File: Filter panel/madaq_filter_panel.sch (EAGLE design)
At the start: 34 parts

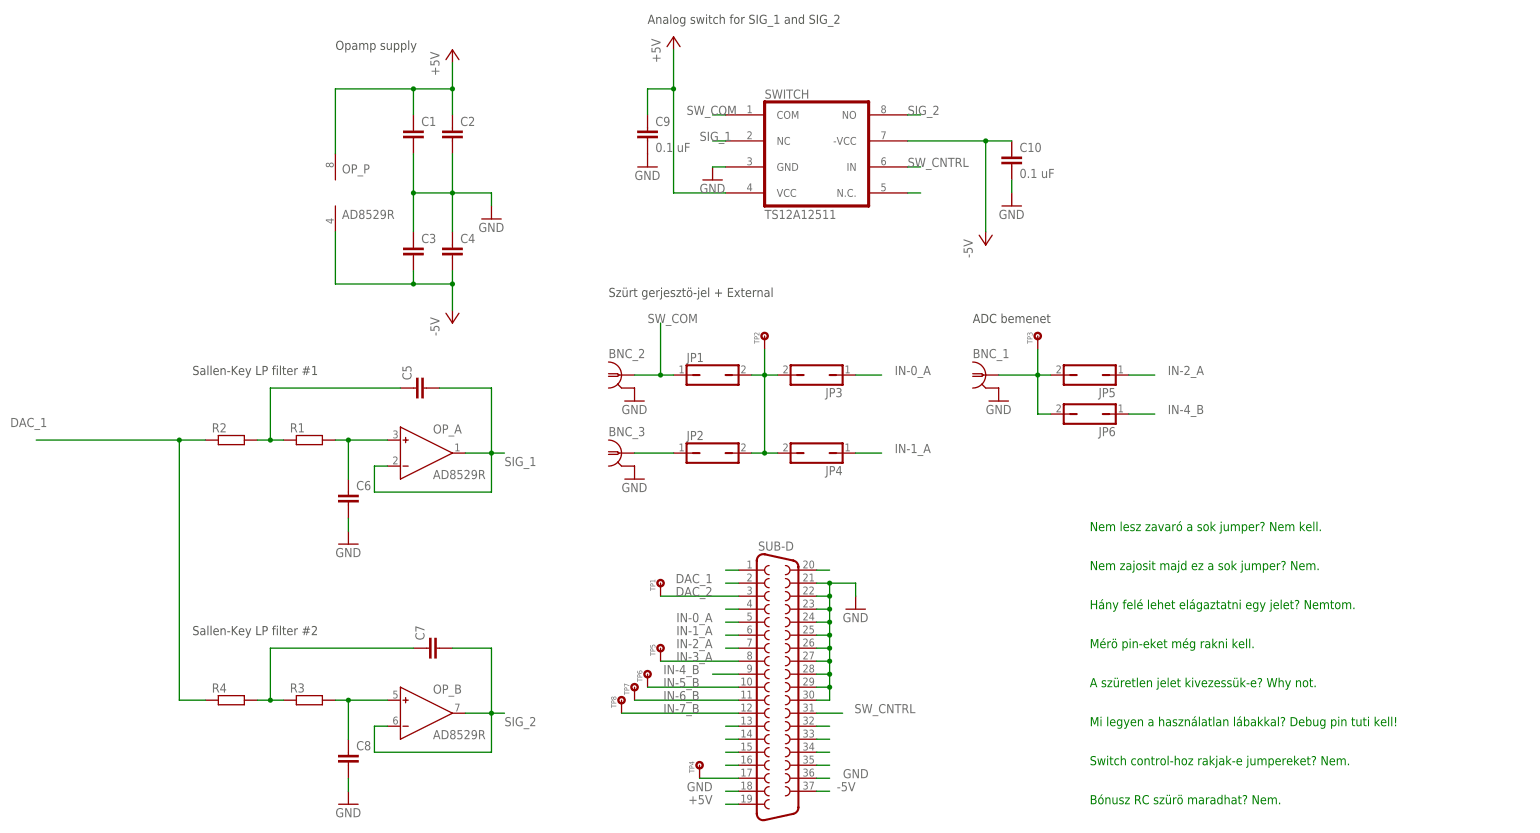
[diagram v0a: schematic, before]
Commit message: Filter panel - V4 sch + brd, Robi és János átnézte - ez nem a megrendelt verzió (János még babrált a board-on)
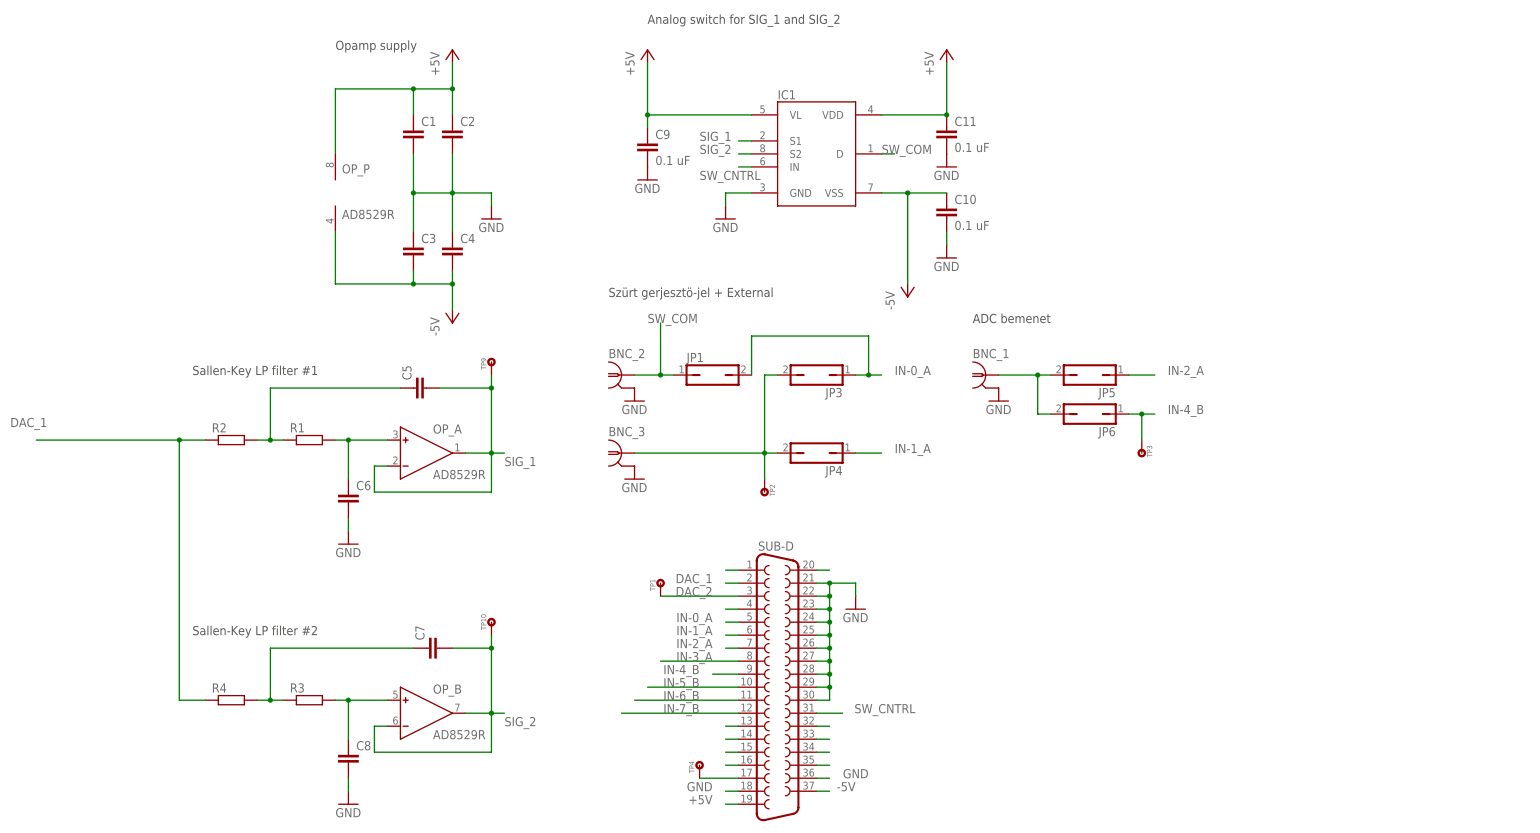
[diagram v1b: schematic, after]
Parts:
- removed JP2: (no value), jumper:JP1Q
- removed SWITCH: TS12A12511, Zoli2_2015-02-22:TS12A12511
- removed TP5, TP6, TP7, TP8: TP, MRobi:TP
- added C11: 0.1 uF, Zoli2_2015-01-28:C1206
- added IC1: (no value), MRobi:ADG419BR
- added TP10, TP9: TP, MRobi:TP
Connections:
- removed net N$2: SWITCH.N.C.
- removed net N$7: JP1.2, JP2.2, JP3.2, JP4.2, TP2.1
- net +5V: now also C11.2, IC1.VDD, IC1.VL; no longer SWITCH.VCC
- net -5V: now also IC1.VSS; no longer SWITCH.-VCC
- net GND: now also C11.1, IC1.GND; no longer SWITCH.GND
- net IN-0_A: now also JP1.2
- net IN-3_A: no longer TP5.1
- net IN-4_B: now also TP3.1
- net IN-5_B: no longer TP6.1
- net IN-6_B: no longer TP7.1
- net IN-7_B: no longer TP8.1
- net N$8: no longer TP3.1
- net N$9: now also JP3.2, JP4.2, TP2.1; no longer JP2.1
- net SIG_1: now also IC1.S1, TP9.1; no longer SWITCH.NC
- net SIG_2: now also IC1.S2, TP10.1; no longer SWITCH.NO
- net SW_CNTRL: now also IC1.IN; no longer SWITCH.IN
- net SW_COM: now also IC1.D; no longer SWITCH.COM
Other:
- note removed: "A szüretlen jelet kivezessük-e? Why not."
- note removed: "Bónusz RC szürö maradhat? Nem."
- note removed: "Hány felé lehet elágaztatni egy jelet? Nemtom."
- note removed: "Mi legyen a használatlan lábakkal? Debug pin tuti kell!"
- note removed: "Mérö pin-eket még rakni kell."
- note removed: "Nem lesz zavaró a sok jumper? Nem kell."
- note removed: "Nem zajosit majd ez a sok jumper? Nem."
- note removed: "Switch control-hoz rakjak-e jumpereket? Nem."
- moved on the sheet: C10, C9, TP2, TP3

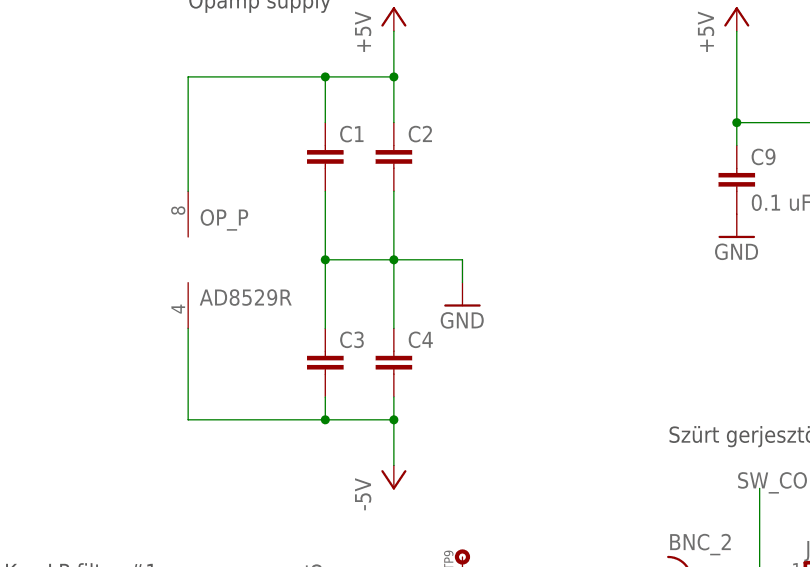
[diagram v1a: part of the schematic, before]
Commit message: Filter panel - János upgraded version, R C értékek még kellenek
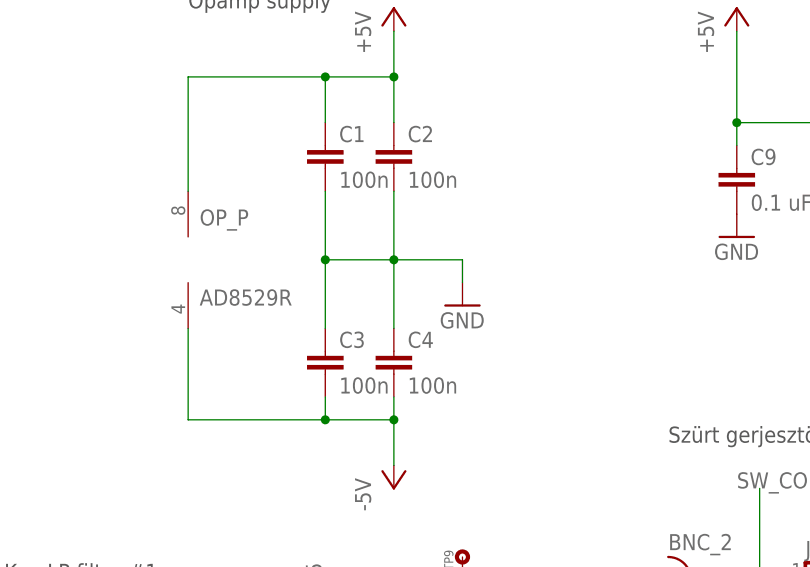
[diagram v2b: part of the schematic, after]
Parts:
- C1, C2, C3, C4: value (none) -> 100n
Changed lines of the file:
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@@
 </classes>
 <parts>
-<part name="C1" library="Zoli2_2015-01-28" deviceset="C" device="1206"/>
-<part name="C2" library="Zoli2_2015-01-28" deviceset="C" device="1206"/>
-<part name="C3" library="Zoli2_2015-01-28" deviceset="C" device="1206"/>
-<part name="C4" library="Zoli2_2015-01-28" deviceset="C" device="1206"/>
+<part name="C1" library="Zoli2_2015-01-28" deviceset="C" device="1206" value="100n"/>
+<part name="C2" library="Zoli2_2015-01-28" deviceset="C" device="1206" value="100n"/>
+<part name="C3" library="Zoli2_2015-01-28" deviceset="C" device="1206" value="100n"/>
+<part name="C4" library="Zoli2_2015-01-28" deviceset="C" device="1206" value="100n"/>
 <part name="GND2" library="supply1" deviceset="GND" device=""/>
 <part name="R1" library="Zoli2_2015-01-28" deviceset="R" device="1206"/>

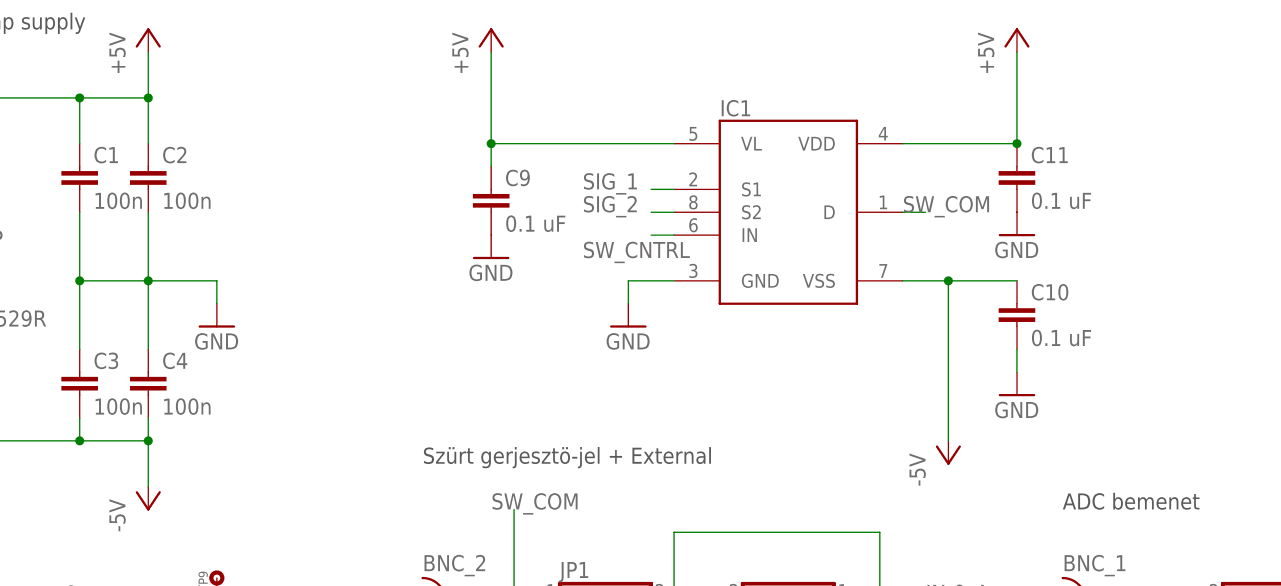
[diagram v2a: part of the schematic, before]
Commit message: Souce - Filter panellel működő kód - P1_3 filter/switch control push pull-ra állítva - kimeneti jel DAC0 helyett DAC1-en megy - @1, @2 adc ch config utasítások
Labview
- több periódust is lehet használni
- optimális izé képletek korrigálva (period <--> samples)

Filter panel
- R,C értékek belőve, megépített verzió
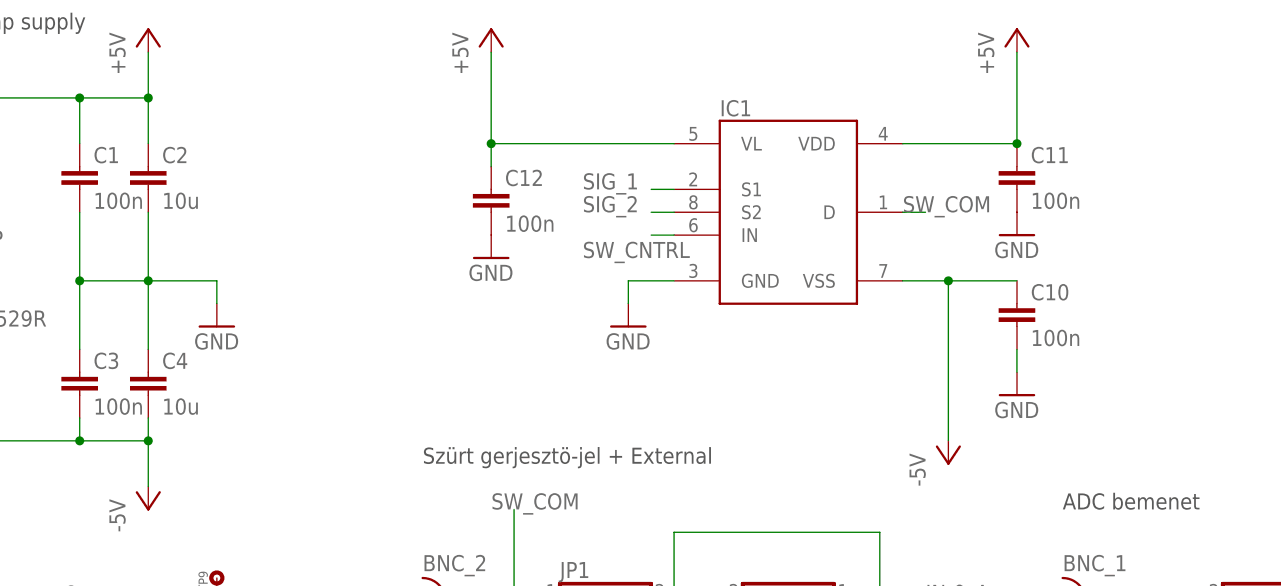
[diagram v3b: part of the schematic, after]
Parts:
- C10, C11, C12: value 0.1 uF -> 100n
- C2, C4: value 100n -> 10u
- renumbered C9 to C12
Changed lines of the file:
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@@
 <parts>
 <part name="C1" library="Zoli2_2015-01-28" deviceset="C" device="1206" value="100n"/>
-<part name="C2" library="Zoli2_2015-01-28" deviceset="C" device="1206" value="100n"/>
+<part name="C2" library="Zoli2_2015-01-28" deviceset="C" device="1206" value="10u"/>
 <part name="C3" library="Zoli2_2015-01-28" deviceset="C" device="1206" value="100n"/>
-<part name="C4" library="Zoli2_2015-01-28" deviceset="C" device="1206" value="100n"/>
+<part name="C4" library="Zoli2_2015-01-28" deviceset="C" device="1206" value="10u"/>
 <part name="GND2" library="supply1" deviceset="GND" device=""/>
 <part name="R1" library="Zoli2_2015-01-28" deviceset="R" device="1206"/>
@@
 <part name="P-2" library="supply1" deviceset="-5V" device=""/>
 <part name="P+2" library="supply1" deviceset="+5V" device=""/>
-<part name="C9" library="Zoli2_2015-01-28" deviceset="C" device="1206" value="0.1 uF"/>
-<part name="C10" library="Zoli2_2015-01-28" deviceset="C" device="1206" value="0.1 uF"/>
+<part name="C12" library="Zoli2_2015-01-28" deviceset="C" device="1206" value="100n"/>
+<part name="C10" library="Zoli2_2015-01-28" deviceset="C" device="1206" value="100n"/>
 <part name="GND5" library="supply1" deviceset="GND" device=""/>
 <part name="GND6" library="supply1" deviceset="GND" device=""/>
@@
 <part name="TP4" library="MRobi" deviceset="TP" device=""/>
 <part name="IC1" library="MRobi" deviceset="ADG419" device="BR"/>
-<part name="C11" library="Zoli2_2015-01-28" deviceset="C" device="1206" value="0.1 uF"/>
+<part name="C11" library="Zoli2_2015-01-28" deviceset="C" device="1206" value="100n"/>
 <part name="P+3" library="supply1" deviceset="+5V" device=""/>
 <part name="GND11" library="supply1" deviceset="GND" device=""/>
@@
 <instance part="P-2" gate="1" x="147.32" y="104.14"/>
 <instance part="P+2" gate="1" x="96.52" y="152.4"/>
-<instance part="C9" gate="G$1" x="96.52" y="134.62"/>
+<instance part="C12" gate="G$1" x="96.52" y="134.62"/>
 <instance part="C10" gate="G$1" x="154.94" y="121.92"/>
 <instance part="GND5" gate="1" x="111.76" y="119.38"/>
@@
 </segment>
 <segment>
-<pinref part="C9" gate="G$1" pin="1"/>
+<pinref part="C12" gate="G$1" pin="1"/>
 <pinref part="GND6" gate="1" pin="GND"/>
 </segment>
@@
 <pinref part="IC1" gate="G$1" pin="VL"/>
 <wire x1="116.84" y1="139.7" x2="96.52" y2="139.7" width="0.1524" layer="91"/>
-<pinref part="C9" gate="G$1" pin="2"/>
+<pinref part="C12" gate="G$1" pin="2"/>
 <wire x1="96.52" y1="137.16" x2="96.52" y2="139.7" width="0.1524" layer="91"/>
 <junction x="96.52" y="139.7"/>
